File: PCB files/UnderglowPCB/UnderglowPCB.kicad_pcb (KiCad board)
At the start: 4 copper layers, 90 x 65 mm, 71 parts, among them J1 Conn_01x03, J10 Conn_01x03, J11 Conn_01x05, J12 Conn_01x07, J2 DB9_Male, J3 USB_B_Micro, J4 Conn_01x03, J5 Conn_01x03, J6 Conn_01x03, J7 Conn_01x03, J8 Conn_01x03, J9 Conn_01x03, Q1 S8050, Q2 S8050, U1 ESP32-WROOM-32D, U2 LMR14030-Q1, U3 NCP1117-3.3_SOT223, U4 TXB0108DQSR, U6 SN65HVD230, U7 USBLC6-2SC6, U8 CP2102N-A01-GQFN28

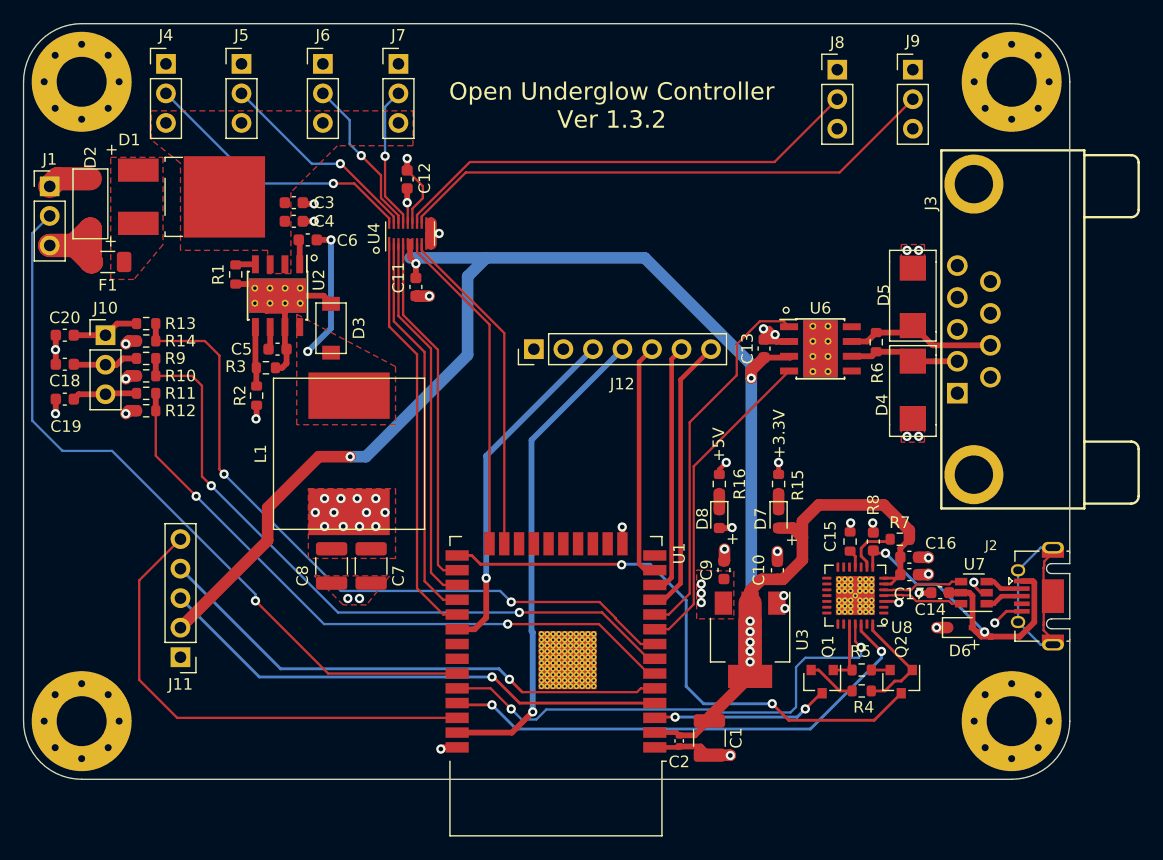
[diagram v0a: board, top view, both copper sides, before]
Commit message: Updated PCB to 1.3.4: silkscreen updates for cathode clarification. Test code moving along.
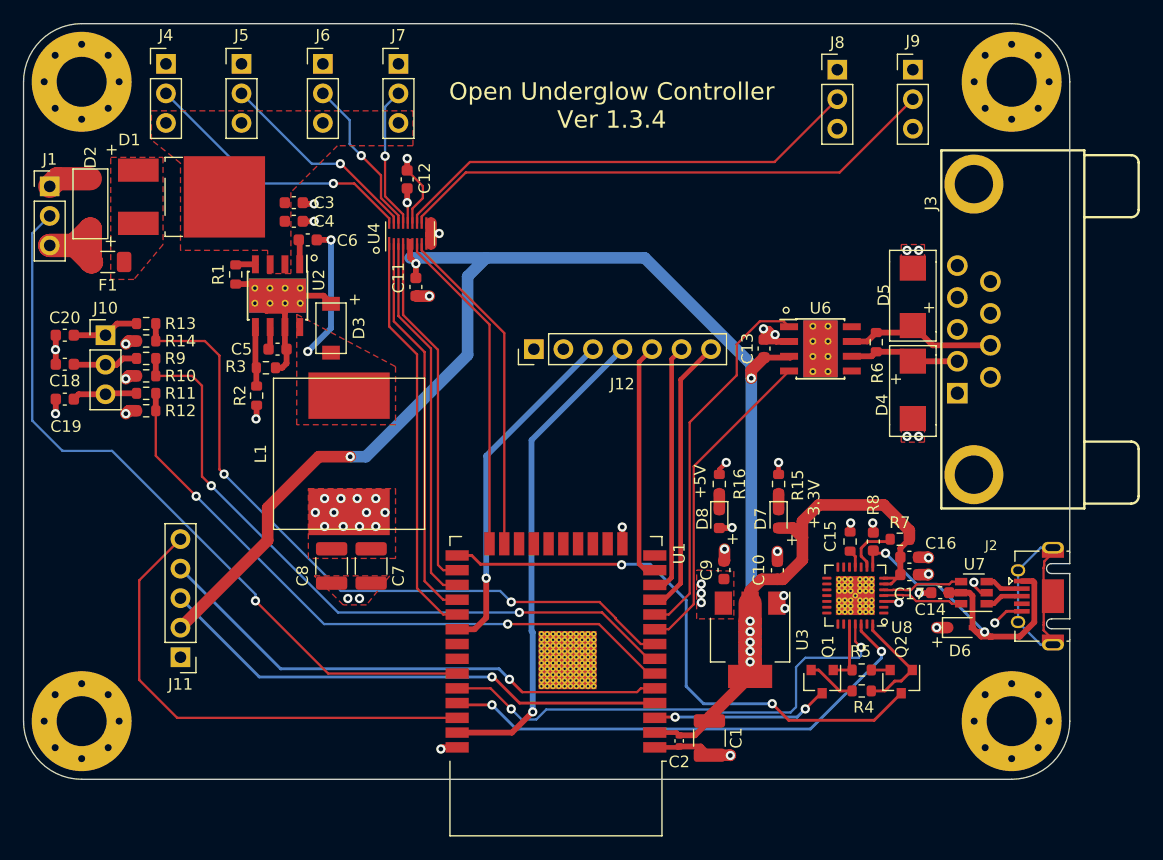
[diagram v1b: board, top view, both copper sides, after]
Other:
- board text added: "Open Underglow Controller Ver 1.3.4"
- board text removed: "Open Underglow Controller Ver 1.3.2"
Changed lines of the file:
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@@
-(kicad_pcb (version 20171130) (host pcbnew 5.1.10-1.fc33)
+(kicad_pcb (version 20171130) (host pcbnew 5.1.10-1.fc34)
   (general
     (thickness 1.6)
-    (drawings 44)
+    (drawings 47)
     (tracks 564)
     (zones 0)
@@
     (title "Open Underglow  Controller")
     (date 2021-05-24)
-    (rev 1.3.2)
+    (rev 1.3.4)
     (company "Jeremy Stintzcum")
   )
@@
       (solder_mask_margin 0.0508))
   )
-  (gr_text "Open Underglow Controller\nVer 1.3.2\n" (at 154.65 75) (layer F.SilkS)
+  (gr_text + (at 179.1 98.5) (layer F.SilkS)
+    (effects (font (size 1 1) (thickness 0.15)))
+  )
+  (gr_text + (at 181.95 92.35) (layer F.SilkS)
+    (effects (font (size 1 1) (thickness 0.15)))
+  )
+  (gr_text + (at 132.55 91.65) (layer F.SilkS)
+    (effects (font (size 1 1) (thickness 0.15)))
+  )
+  (gr_text "Open Underglow Controller\nVer 1.3.4\n" (at 154.65 75) (layer F.SilkS)
     (effects (font (size 1.5 1.5) (thickness 0.2)))
   )
@@
   (gr_line (start 109.05 67.95) (end 189.05 67.95) (layer Edge.Cuts) (width 0.05))
   (gr_circle (center 178.1 119.4) (end 177.85 119.4) (layer F.SilkS) (width 0.12))
-  (gr_text + (at 185.85 121.4 180) (layer F.SilkS)
+  (gr_text + (at 182.65 121.2 180) (layer F.SilkS)
     (effects (font (size 1 1) (thickness 0.15)))
   )
@@
   )
   (gr_circle (center 169.65 92.6) (end 169.65 92.85) (layer F.SilkS) (width 0.12))
-  (gr_text +3.3V (at 169.05 103.25 90) (layer F.SilkS)
+  (gr_text +3.3V (at 172.05 109.3 90) (layer F.SilkS)
     (effects (font (size 1 1) (thickness 0.15)))
   )
-  (gr_text +5V (at 163.85 104.15 90) (layer F.SilkS)
+  (gr_text +5V (at 162.25 107.35 90) (layer F.SilkS)
     (effects (font (size 1 1) (thickness 0.15)))
   )
